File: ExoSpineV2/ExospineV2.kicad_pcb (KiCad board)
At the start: 2 copper layers, 79.5 x 73.1 mm, 51 parts, among them J1 GPIO, J15 JST PH 3pin, J16 JST PH 3pin, J2 2.54mm 4pin, J3 JST PH 3pin, J31 JST PH 3pin, J32 JST PH 3pin, J33 JST PH 3pin, J34 JST PH 3pin, J35 JST PH 3pin, J36 JST PH 3pin, J4 JST PH 4pin, J41 JST PH 3pin, J42 JST PH 3pin, J5 JST PH 2pin, J51 JST PH 4pin, J52 JST PH 3pin, J53 JST PH 4pin, J54 JST PH 3pin, J55 JST PH 4pin, J56 JST PH 3pin, J6 JST PH 2pin, J7 JST PH 3pin, J8 JST PH 2pin, J9 JST PH 2pin, U1 MCP3008-I/SL, U2 74HC00D,653, U3 74HC00D,653

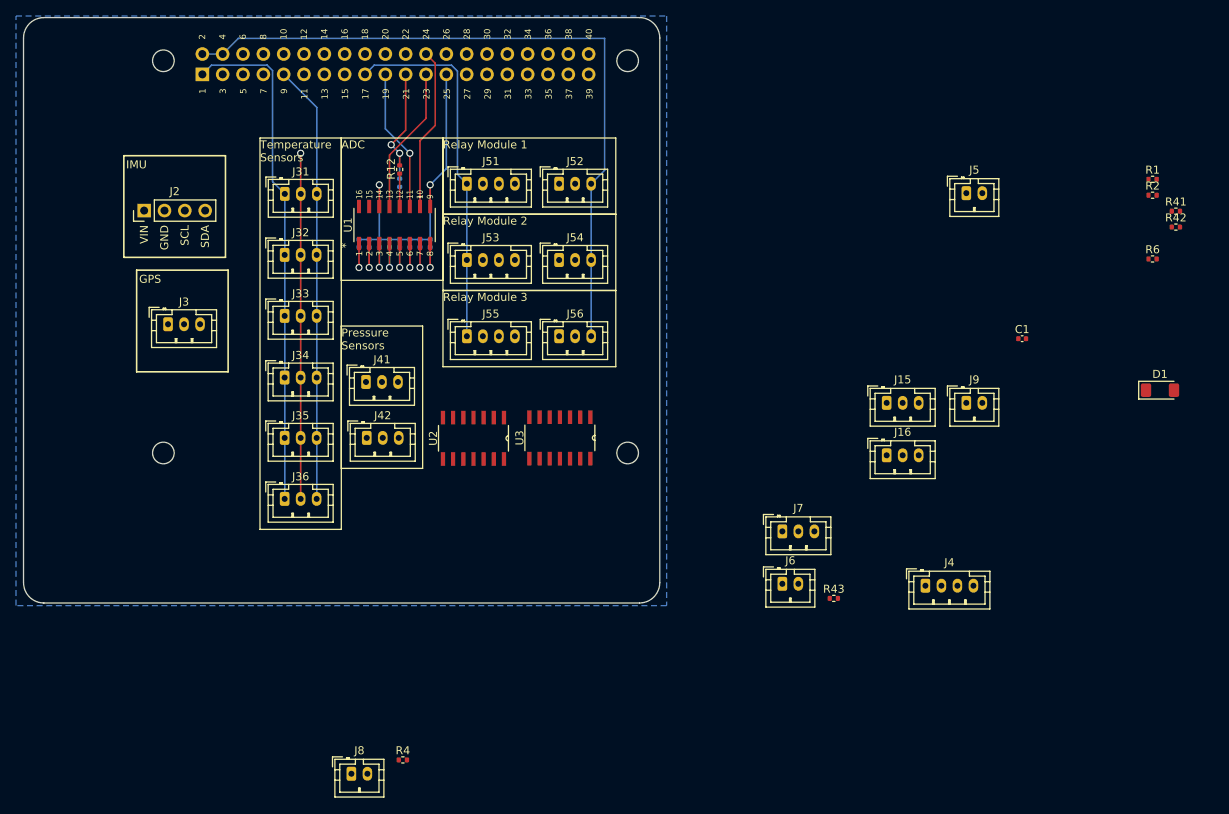
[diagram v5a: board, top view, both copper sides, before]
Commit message: placed some components on PCB
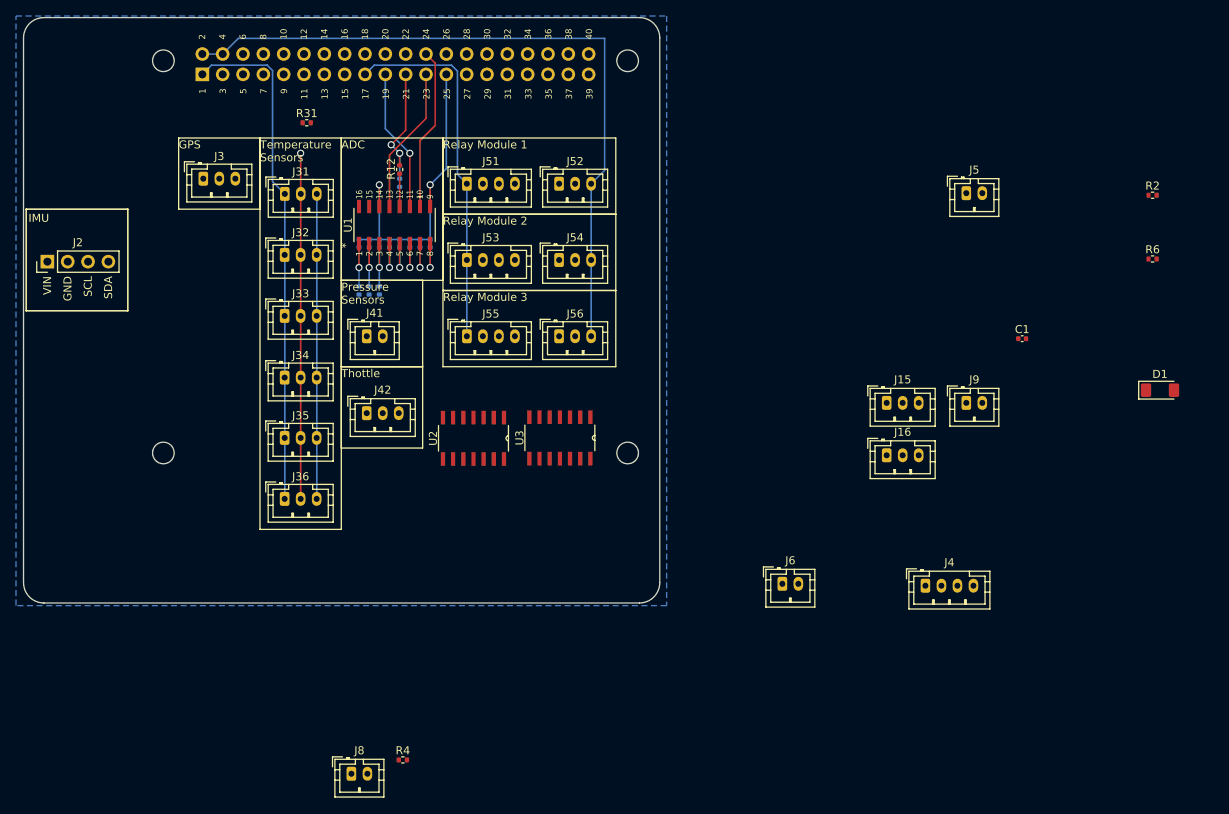
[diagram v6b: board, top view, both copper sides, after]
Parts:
- removed the J42 at (128.9, 94.6)
- J41: value JST PH 3pin -> JST PH 2pin; footprint Connector_JST:JST_PH_B3B-PH-K_1x03_P2.00mm_Vertical -> Connector_JST:JST_PH_B2B-PH-K_1x02_P2.00mm_Vertical
- R41, R42, R43: moved to B.Cu
- moved R31 105.9 mm to (121.4, 55.2)
- moved R41 102.5 mm to (127.9, 76.2), turned to 90 degrees
- moved R42 101.1 mm to (129.2, 76.2), turned to 90 degrees
- moved R43 68.6 mm to (130.5, 76.2), turned to 90 degrees
- moved J42 54.0 mm to (128.9, 91.5)
- moved J3 18.7 mm to (108.5, 62.2)
- moved J2 13.7 mm to (89.0, 72.6)
- moved J41 5.72 mm to (128.9, 81.9)
- renumbered J7 to J42, R1 to R31
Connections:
- J41 pad 1: +24V -> /MCP3008.CH0
- J41 pad 2: /MCP3008.CH0 -> /MCP3008.CH1
- U2 pad 11: /GPIO5 -> /GPIO21/PCM.DOUT
- U3 pad 11: /GPIO6 -> /GPIO21/PCM.DOUT
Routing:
- net GND: track 98.0 -> 81.3 mm
- net /MCP3008.CH2: track 5.54 -> 7.90 mm
- net /MCP3008.CH1: track 5.54 -> 7.90 mm
- net /MCP3008.CH0: track 5.54 -> 7.90 mm
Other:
- board text added: "Thottle"

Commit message: Kicad 8
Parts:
- moved J2 2.89 mm to (91.8, 73.4)

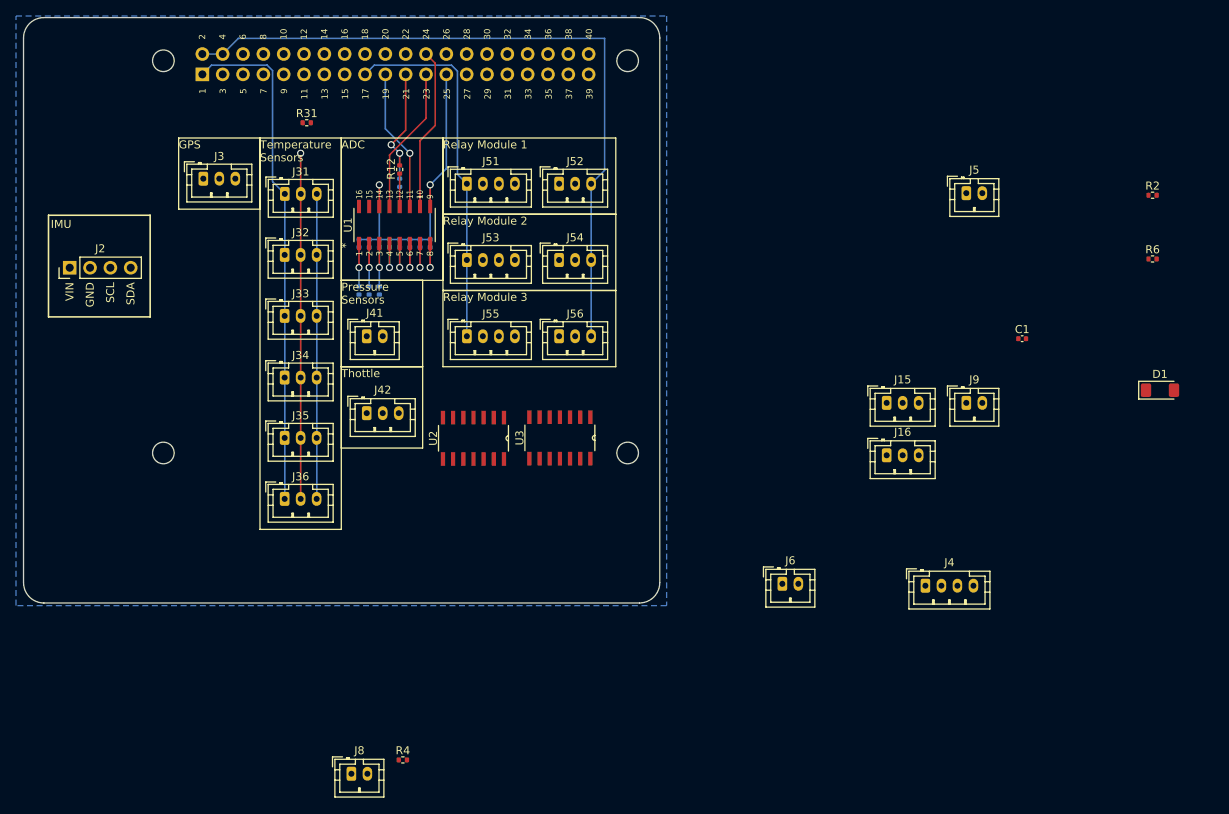
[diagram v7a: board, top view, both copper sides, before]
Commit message: sized traces (Power/default)
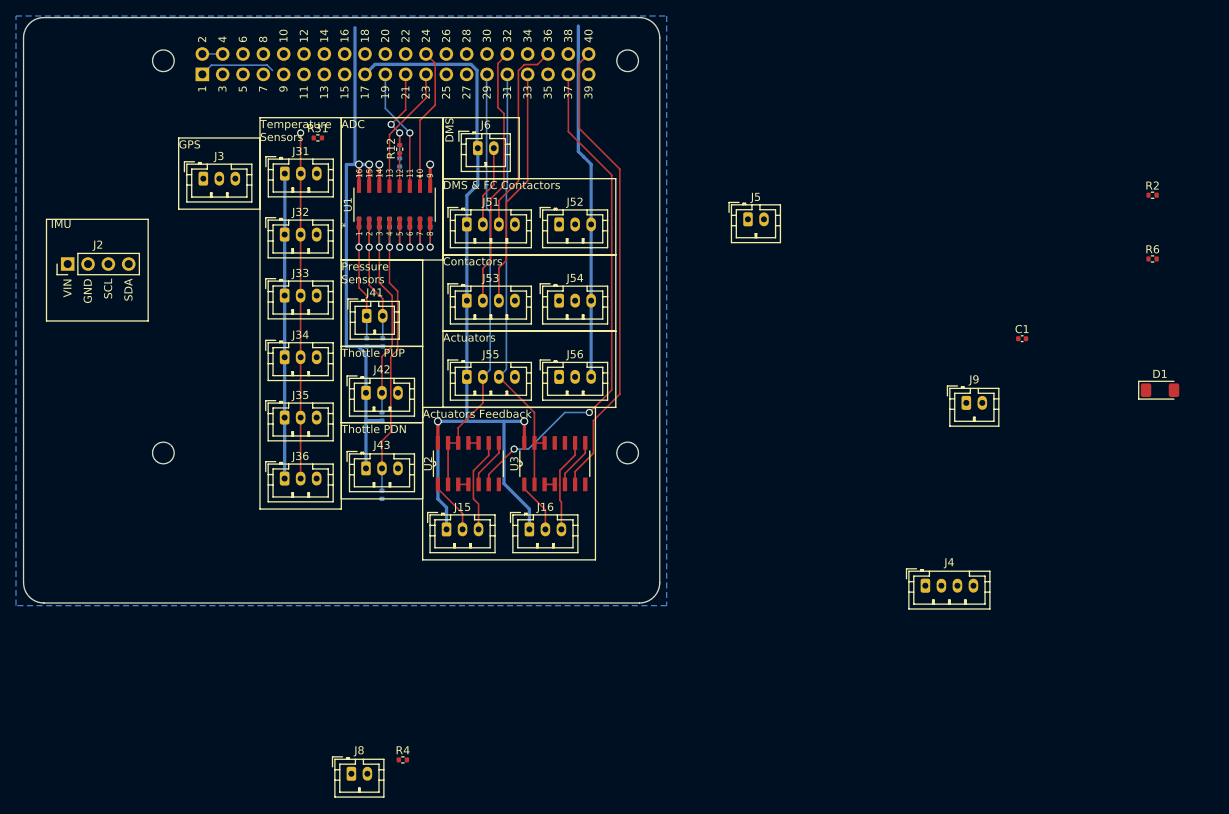
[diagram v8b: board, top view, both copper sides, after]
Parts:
- added J43: JST PH 3pin, Connector_JST:JST_PH_B3B-PH-K_1x03_P2.00mm_Vertical, F.Cu at (128.8, 98.4)
- added R44: 10k, Resistor_SMD:R_0402_1005Metric, B.Cu at (130.8, 101.7)
- moved J6 66.4 mm to (142.8, 58.4)
- moved J15 57.2 mm to (138.9, 106.0)
- moved J16 45.6 mm to (149.2, 106.0)
- moved J5 27.5 mm to (176.5, 67.3)
- moved R43 15.8 mm to (130.8, 92.0)
- moved R42 6.69 mm to (130.9, 82.7)
- moved R41 6.55 mm to (128.9, 82.7)
- moved J53 5.08 mm to (141.4, 77.5)
- moved J54 5.08 mm to (152.9, 77.5)
- moved J55 5.08 mm to (141.4, 87.0)
- moved J56 5.08 mm to (152.9, 87.0)
- moved J51 5.08 mm to (141.4, 67.9)
- moved J52 5.08 mm to (152.9, 67.9)
- moved U3 3.29 mm to (152.4, 97.8), turned to 90 degrees
- moved U2 3.24 mm to (141.6, 97.8), turned to 90 degrees
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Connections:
- J51 pad 2: /GPIO12 -> /DMS
- J51 pad 3: /GPIO13 -> /GPIO16
- J53 pad 2: /DMS -> /GPIO12/PWM0
- J53 pad 3: /GPIO16 -> /GPIO13/PWM1
- U2 pad 10: Net-(J15-Pin_3) -> Net-(U2-Pad10)
- U2 pad 11: /GPIO21/PCM.DOUT -> Net-(U2-Pad10)
- U2 pad 12: Net-(U2-3Y) -> /GPIO5
- U2 pad 13: Net-(U2-1Y) -> /GPIO5
- U2 pad 2: /GPIO23 -> /GPIO5
- U2 pad 3: Net-(U2-1Y) -> Net-(U2-Pad3)
- U2 pad 4: /GPIO23 -> Net-(U2-Pad3)
- U2 pad 5: /GPIO23 -> Net-(U2-Pad5)
- U2 pad 6: Net-(U2-2Y) -> /GPIO26
- U2 pad 8: Net-(U2-3Y) -> Net-(U2-Pad5)
- U2 pad 9: Net-(U2-2Y) -> Net-(J15-Pin_3)
- U3 pad 10: Net-(J16-Pin_3) -> Net-(U3-3B)
- U3 pad 11: /GPIO21/PCM.DOUT -> Net-(U3-3B)
- U3 pad 12: Net-(U3-3Y) -> /GPIO6
- U3 pad 13: Net-(U3-1Y) -> /GPIO6
- U3 pad 2: /GPIO24 -> /GPIO6
- U3 pad 4: /GPIO24 -> Net-(U3-1Y)
- U3 pad 5: /GPIO24 -> Net-(U3-2B)
- U3 pad 6: Net-(U3-2Y) -> /GPIO21/PCM.DOUT
- U3 pad 8: Net-(U3-3Y) -> Net-(U3-2B)
- U3 pad 9: Net-(U3-2Y) -> Net-(J16-Pin_3)
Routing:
- net GND: track 81.3 -> 6.08 mm
- net /GPIO26: track 0.00 -> 62.7 mm, vias 0 -> 2
- net /GPIO21/PCM.DOUT: track 0.00 -> 58.7 mm
- net /GPIO6: track 0.00 -> 54.8 mm
- net /GPIO5: track 0.00 -> 54.4 mm
- net +3.3V: track 109.6 -> 151.9 mm, vias 0 -> 2
- net /GPIO12/PWM0: track 0.00 -> 32.7 mm
- net /MCP3008.CH3: track 5.54 -> 37.2 mm
- net /GPIO13/PWM1: track 0.00 -> 29.8 mm
- net +5V: track 89.0 -> 117.3 mm, vias 0 -> 2
- net /GPIO16: track 0.00 -> 24.8 mm
- net /MCP3008.CH2: track 7.90 -> 27.4 mm
- net Net-(J15-Pin_3): track 0.00 -> 11.8 mm
- net Net-(J16-Pin_3): track 0.00 -> 11.7 mm
- net /DMS: track 0.00 -> 10.1 mm
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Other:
- board text added: "1"
- board text added: "10"
- board text added: "11"
- board text added: "12"
- board text added: "13"
- board text added: "14"
- board text added: "15"
- board text added: "16"
- board text added: "17"
- board text added: "18"
- board text added: "19"
- board text added: "2"
- board text added: "20"
- board text added: "21"
- board text added: "22"
- board text added: "23"
- board text added: "24"
- board text added: "25"
- board text added: "26"
- board text added: "27"
- board text added: "28"
- board text added: "29"
- board text added: "3"
- board text added: "30"
- board text added: "31"
- board text added: "32"
- board text added: "33"
- board text added: "34"
- board text added: "35"
- board text added: "36"
- board text added: "37"
- board text added: "38"
- board text added: "39"
- board text added: "4"
- board text added: "40"
- board text added: "5"
- board text added: "6"
- board text added: "7"
- board text added: "8"
- board text added: "9"
- board text added: "Actuators"
- board text added: "Actuators Feedback"
- board text added: "Contactors"
- board text added: "DMS"
- board text added: "DMS & FC Contactors"
- board text added: "Thottle PDN"
- board text added: "Thottle PUP"
- board text removed: "1 3 5 7 9 11 13 15 17 19 21 23 25 27 29 31 33 35 37 39"
- board text removed: "2 4 6 8 10 12 14 16 18 20 22 24 26 28 30 32 34 36 38 40"
- board text removed: "Relay Module 1"
- board text removed: "Relay Module 2"
- board text removed: "Relay Module 3"
- board text removed: "Thottle"
